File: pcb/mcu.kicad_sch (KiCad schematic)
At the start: 28 parts, among them CN9 2x5, IC2 STM32f103C8T, X1 H130B-8.000-18-3030-EXT-TR, X2 32.768K12.5PI/MC306

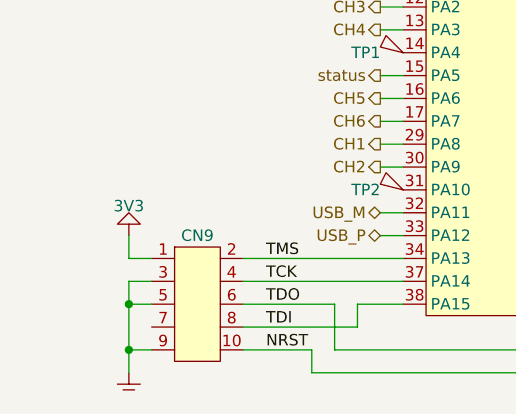
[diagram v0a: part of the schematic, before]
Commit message: worked on layout. changed JTAG pinout and changed it to bottomside test-points
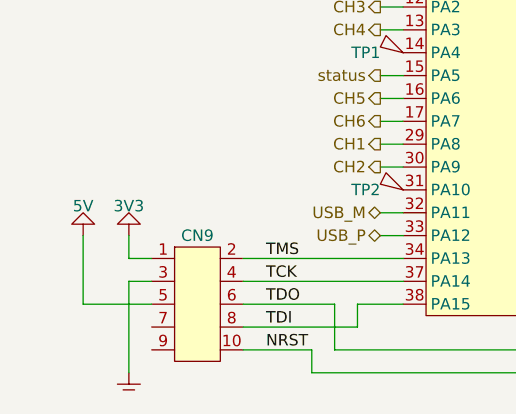
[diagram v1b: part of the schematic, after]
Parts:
- CN9: footprint pin_headers:2x5 -> pin_headers:2x5_test_points
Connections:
- net GND: no longer CN9.5, CN9.9
- new net 5V: CN9.5
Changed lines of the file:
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@@
   (junction (at 132.08 68.58) (diameter 0) (color 0 0 0 0)
   )
-  (junction (at 104.14 134.62) (diameter 0) (color 0 0 0 0)
-  )
   (junction (at 180.34 83.82) (diameter 0) (color 0 0 0 0)
   )
@@
   (junction (at 114.3 76.2) (diameter 0) (color 0 0 0 0)
   )
-  (junction (at 104.14 139.7) (diameter 0) (color 0 0 0 0)
-  )
   (junction (at 177.8 66.04) (diameter 0) (color 0 0 0 0)
   )
@@
     (stroke (width 0) (type default))
   )
-  (wire (pts (xy 104.14 139.7) (xy 106.68 139.7))
-    (stroke (width 0) (type default))
-  )
   (wire (pts (xy 114.3 73.66) (xy 114.3 76.2))
     (stroke (width 0) (type default))
@@
     (stroke (width 0) (type default))
   )
+  (wire (pts (xy 99.06 127) (xy 99.06 134.62))
+    (stroke (width 0) (type default))
+  )
   (wire (pts (xy 132.08 68.58) (xy 134.62 68.58))
     (stroke (width 0) (type default))
@@
     (stroke (width 0) (type default))
   )
-  (wire (pts (xy 104.14 134.62) (xy 106.68 134.62))
-    (stroke (width 0) (type default))
-  )
   (wire (pts (xy 165.1 66.04) (xy 177.8 66.04))
     (stroke (width 0) (type default))
@@
     (stroke (width 0) (type default))
   )
+  (wire (pts (xy 99.06 134.62) (xy 106.68 134.62))
+    (stroke (width 0) (type default))
+  )
   (wire (pts (xy 132.08 114.3) (xy 134.62 114.3))
     (stroke (width 0) (type default))
@@
     (stroke (width 0) (type default))
   )
-  (wire (pts (xy 104.14 132.08) (xy 104.14 134.62))
+  (wire (pts (xy 104.14 132.08) (xy 104.14 142.24))
     (stroke (width 0) (type default))
   )
@@
     (stroke (width 0) (type default))
   )
-  (wire (pts (xy 104.14 139.7) (xy 104.14 134.62))
-    (stroke (width 0) (type default))
-  )
   (wire (pts (xy 160.02 121.92) (xy 162.56 121.92))
     (stroke (width 0) (type default))
@@
   )
   (wire (pts (xy 185.42 83.82) (xy 187.96 83.82))
-    (stroke (width 0) (type default))
-  )
-  (wire (pts (xy 104.14 142.24) (xy 104.14 139.7))
     (stroke (width 0) (type default))
   )
@@
     )
   )
+  (symbol (lib_id "generic:5V") (at 99.06 127 0) (unit 1)
+    (in_bom yes) (on_board yes) (dnp no)
+    (property "Reference" "#5V03" (at 102.87 125.73 0)
+      (effects (font (size 1.27 1.27)) hide)
+    )
+    (property "Value" "5V" (at 99.06 124.46 0)
+      (effects (font (size 1.27 1.27)) (justify bottom))
+    )
+    (property "Footprint" "" (at 99.06 127 0)
+      (effects (font (size 1.27 1.27)) hide)
+    )
+    (property "Datasheet" "" (at 99.06 127 0)
+      (effects (font (size 1.27 1.27)) hide)
+    )
+    (pin "~")
+    (instances
+      (project "pcb"
+        (path "/6bb3bad6-1a89-4624-b34d-6ddda7dd16d2"
+          (reference "#5V03") (unit 1)
+        )
+        (path "/6bb3bad6-1a89-4624-b34d-6ddda7dd16d2/19469851-aeaf-466c-9786-c0d0ae531cf4"
+          (reference "#5V02") (unit 1)
+        )
+      )
+    )
+  )
   (symbol (lib_id "PCB:test_point") (at 180.34 114.3 0) (unit 1)
     (in_bom yes) (on_board yes) (dnp no) (fields_autoplaced)
@@
       (effects (font (size 1.27 1.27)) hide)
     )
-    (property "Footprint" "pin_headers:2x5" (at 106.68 129.54 0)
-      (effects (font (size 1.27 1.27)) hide)
-    )
+    (property "Footprint" "pin_headers:2x5_test_points" (at 106.68 129.54 0)
+      (effects (font (size 1.27 1.27)) hide)
+    )

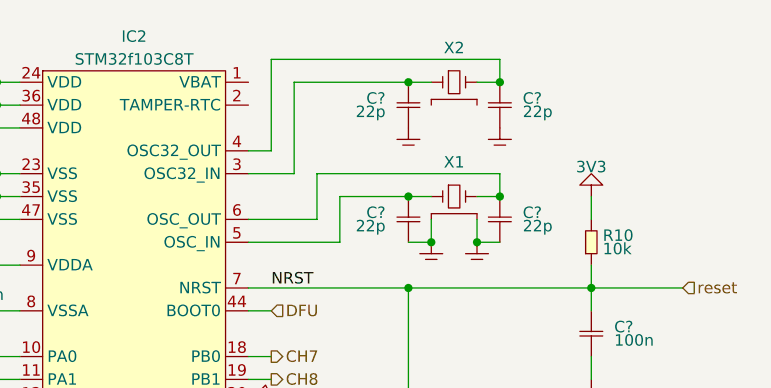
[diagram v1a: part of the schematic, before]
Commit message: removed RTC crystal, started routing
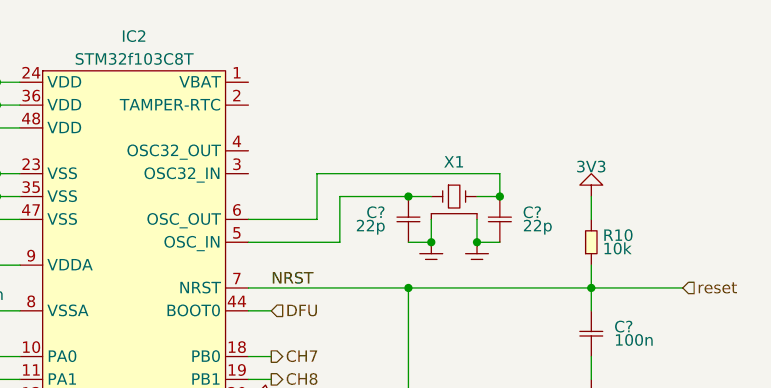
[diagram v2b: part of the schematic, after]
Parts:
- removed C? (x2): 22p, SMT:0603, symbol generic:C
- removed X2: 32.768K12.5PI/MC306, xtal:8x3.2, symbol oscillators:32.768K12.5PI/MC306
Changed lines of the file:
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@@
     (comment 1 "Microcontroller and programming headers")
   )
-  (junction (at 187.96 66.04) (diameter 0) (color 0 0 0 0)
-  )
   (junction (at 127 91.44) (diameter 0) (color 0 0 0 0)
   )
@@
   (junction (at 114.3 76.2) (diameter 0) (color 0 0 0 0)
   )
-  (junction (at 177.8 66.04) (diameter 0) (color 0 0 0 0)
-  )
   (junction (at 127 86.36) (diameter 0) (color 0 0 0 0)
   )
@@
     (stroke (width 0) (type default))
   )
-  (wire (pts (xy 160.02 73.66) (xy 162.56 73.66))
-    (stroke (width 0) (type default))
-  )
   (wire (pts (xy 127 139.7) (xy 175.26 139.7))
     (stroke (width 0) (type default))
@@
     (stroke (width 0) (type default))
   )
-  (wire (pts (xy 177.8 66.04) (xy 180.34 66.04))
-    (stroke (width 0) (type default))
-  )
   (wire (pts (xy 160.02 111.76) (xy 180.34 111.76))
     (stroke (width 0) (type default))
@@
     (stroke (width 0) (type default))
   )
-  (wire (pts (xy 165.1 76.2) (xy 165.1 66.04))
-    (stroke (width 0) (type default))
-  )
-  (wire (pts (xy 162.56 73.66) (xy 162.56 63.5))
-    (stroke (width 0) (type default))
-  )
   (wire (pts (xy 116.84 132.08) (xy 134.62 132.08))
     (stroke (width 0) (type default))
@@
     (stroke (width 0) (type default))
   )
-  (wire (pts (xy 165.1 66.04) (xy 177.8 66.04))
-    (stroke (width 0) (type default))
-  )
   (wire (pts (xy 177.8 78.74) (xy 180.34 78.74))
     (stroke (width 0) (type default))
   )
-  (wire (pts (xy 187.96 63.5) (xy 187.96 66.04))
-    (stroke (width 0) (type default))
-  )
   (wire (pts (xy 116.84 139.7) (xy 124.46 139.7))
     (stroke (width 0) (type default))
@@
     (stroke (width 0) (type default))
   )
-  (wire (pts (xy 162.56 63.5) (xy 187.96 63.5))
-    (stroke (width 0) (type default))
-  )
   (wire (pts (xy 167.64 81.28) (xy 160.02 81.28))
     (stroke (width 0) (type default))
@@
     (stroke (width 0) (type default))
   )
-  (wire (pts (xy 160.02 76.2) (xy 165.1 76.2))
-    (stroke (width 0) (type default))
-  )
   (wire (pts (xy 93.98 76.2) (xy 93.98 73.66))
     (stroke (width 0) (type default))
@@
   )
   (wire (pts (xy 185.42 83.82) (xy 187.96 83.82))
-    (stroke (width 0) (type default))
-  )
-  (wire (pts (xy 185.42 66.04) (xy 187.96 66.04))
     (stroke (width 0) (type default))
   )
@@
     )
   )
-  (symbol (lib_id "oscillators:32.768K12.5PI/MC306") (at 182.88 66.04 0) (unit 1)
-    (in_bom yes) (on_board yes) (dnp no)
-    (property "Reference" "X2" (at 182.88 62.23 0)
-      (effects (font (size 1.27 1.27)))
-    )
-    (property "Value" "32.768K12.5PI/MC306" (at 182.88 66.04 0)
-      (effects (font (size 1.27 1.27)) hide)
-    )
-    (property "Footprint" "xtal:8x3.2" (at 182.88 49.53 0)
-      (effects (font (size 1.27 1.27)) hide)
-    )
-    (property "Datasheet" "https://www.yic.com.tw/wp-content/uploads/2023/11/YIC-MC306-Series.pdf" (at 182.88 57.15 0)
-      (effects (font (size 1.27 1.27)) hide)
-    )
-    (property "MPN" "32.768K12.5PI/MC306" (at 182.88 52.07 0)
-      (effects (font (size 1.27 1.27)) hide)
-    )
-    (property "DigiKey" "3155-32.768K12.5PI/MC306CT-ND" (at 182.88 54.61 0)
-      (effects (font (size 1.27 1.27)) hide)
-    )
-    (pin "1")
-    (pin "2")
-    (pin "3")
-    (pin "4")
-    (instances
-      (project "pcb"
-        (path "/6bb3bad6-1a89-4624-b34d-6ddda7dd16d2/19469851-aeaf-466c-9786-c0d0ae531cf4"
-          (reference "X2") (unit 1)
-        )
-      )
-    )
-  )
   (symbol (lib_id "generic:C") (at 114.3 71.12 0) (unit 1)
     (in_bom yes) (on_board yes) (dnp no)
@@
     )
   )
-  (symbol (lib_id "generic:C") (at 177.8 68.58 0) (mirror y) (unit 1)
-    (in_bom yes) (on_board yes) (dnp no)
-    (property "Reference" "C?" (at 175.26 68.58 0)
+  (symbol (lib_id "generic:C") (at 187.96 81.28 0) (unit 1)
+    (in_bom yes) (on_board yes) (dnp no)
+    (property "Reference" "C?" (at 190.5 81.28 0)
       (effects (font (size 1.27 1.27)) (justify left bottom))
     )
-    (property "Value" "22p" (at 175.26 68.58 0)
+    (property "Value" "22p" (at 190.5 81.28 0)
       (effects (font (size 1.27 1.27)) (justify left top))
     )
-    (property "Footprint" "SMT:0603" (at 177.8 71.12 0)
-      (effects (font (size 1.27 1.27)) hide)
-    )
-    (property "Datasheet" "" (at 177.8 68.58 0)
+    (property "Footprint" "SMT:0603" (at 187.96 83.82 0)
+      (effects (font (size 1.27 1.27)) hide)
+    )
+    (property "Datasheet" "" (at 187.96 81.28 0)
       (effects (font (size 1.27 1.27)) hide)
     )
@@
         )
         (path "/6bb3bad6-1a89-4624-b34d-6ddda7dd16d2/19469851-aeaf-466c-9786-c0d0ae531cf4"
-          (reference "C18") (unit 1)
-        )
-      )
-    )
-  )
-  (symbol (lib_id "generic:C") (at 187.96 81.28 0) (unit 1)
-    (in_bom yes) (on_board yes) (dnp no)
-    (property "Reference" "C?" (at 190.5 81.28 0)
-      (effects (font (size 1.27 1.27)) (justify left bottom))
-    )
-    (property "Value" "22p" (at 190.5 81.28 0)
-      (effects (font (size 1.27 1.27)) (justify left top))
-    )
-    (property "Footprint" "SMT:0603" (at 187.96 83.82 0)
-      (effects (font (size 1.27 1.27)) hide)
-    )
-    (property "Datasheet" "" (at 187.96 81.28 0)
-      (effects (font (size 1.27 1.27)) hide)
-    )
-    (pin "1")
-    (pin "2")
-    (instances
-      (project "pcb"
-        (path "/6bb3bad6-1a89-4624-b34d-6ddda7dd16d2/bd5ce3a2-965f-4825-a529-9d15232fee93"
-          (reference "C?") (unit 1)
-        )
-        (path "/6bb3bad6-1a89-4624-b34d-6ddda7dd16d2/19469851-aeaf-466c-9786-c0d0ae531cf4"
           (reference "C16") (unit 1)
         )
@@
         (path "/6bb3bad6-1a89-4624-b34d-6ddda7dd16d2/19469851-aeaf-466c-9786-c0d0ae531cf4"
           (reference "#3V02") (unit 1)
-        )
-      )
-    )
-  )
-  (symbol (lib_id "generic:C") (at 187.96 68.58 0) (unit 1)
-    (in_bom yes) (on_board yes) (dnp no)
-    (property "Reference" "C?" (at 190.5 68.58 0)
-      (effects (font (size 1.27 1.27)) (justify left bottom))
-    )
-    (property "Value" "22p" (at 190.5 68.58 0)
-      (effects (font (size 1.27 1.27)) (justify left top))
-    )
-    (property "Footprint" "SMT:0603" (at 187.96 71.12 0)
-      (effects (font (size 1.27 1.27)) hide)
-    )
-    (property "Datasheet" "" (at 187.96 68.58 0)
-      (effects (font (size 1.27 1.27)) hide)
-    )
-    (pin "1")
-    (pin "2")
-    (instances
-      (project "pcb"
-        (path "/6bb3bad6-1a89-4624-b34d-6ddda7dd16d2/bd5ce3a2-965f-4825-a529-9d15232fee93"
-          (reference "C?") (unit 1)
-        )
-        (path "/6bb3bad6-1a89-4624-b34d-6ddda7dd16d2/19469851-aeaf-466c-9786-c0d0ae531cf4"
-          (reference "C19") (unit 1)
         )
       )
@@
     )
   )
-  (symbol (lib_id "generic:GND") (at 187.96 71.12 0) (unit 1)
-    (in_bom yes) (on_board yes) (dnp no) (fields_autoplaced)
-    (property "Reference" "#GND025" (at 191.77 69.85 0)
-      (effects (font (size 1.27 1.27)) hide)
-    )
-    (property "Value" "GND" (at 191.77 71.12 0)
-      (effects (font (size 1.27 1.27)) hide)
-    )
-    (property "Footprint" "" (at 187.96 71.12 0)
-      (effects (font (size 1.27 1.27)) hide)
-    )
-    (property "Datasheet" "" (at 187.96 71.12 0)
-      (effects (font (size 1.27 1.27)) hide)
-    )
-    (pin "~")
-    (instances
-      (project "pcb"
-        (path "/6bb3bad6-1a89-4624-b34d-6ddda7dd16d2/19469851-aeaf-466c-9786-c0d0ae531cf4"
-          (reference "#GND025") (unit 1)
-        )
-      )
-    )
-  )
   (symbol (lib_id "generic:GND") (at 116.84 93.98 0) (unit 1)
     (in_bom yes) (on_board yes) (dnp no) (fields_autoplaced)
@@
         )
       )
-    )
-  )
-  (symbol (lib_id "generic:GND") (at 177.8 71.12 0) (unit 1)
-    (in_bom yes) (on_board yes) (dnp no) (fields_autoplaced)
-    (property "Reference" "#GND024" (at 181.61 69.85 0)
-      (effects (font (size 1.27 1.27)) hide)
-    )
-    (property "Value" "GND" (at 181.61 71.12 0)
-      (effects (font (size 1.27 1.27)) hide)
-    )
-    (property "Footprint" "" (at 177.8 71.12 0)
-      (effects (font (size 1.27 1.27)) hide)
-    )
-    (property "Datasheet" "" (at 177.8 71.12 0)
-      (effects (font (size 1.27 1.27)) hide)
-    )
-    (pin "~")
-    (instances
-      (project "pcb"
-        (path "/6bb3bad6-1a89-4624-b34d-6ddda7dd16d2/19469851-aeaf-466c-9786-c0d0ae531cf4"
-          (reference "#GND024") (unit 1)
-        )
-      )

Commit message: routing completed
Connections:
- net USB_M renamed USB_N
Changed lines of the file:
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@@
     (effects (font (size 1.27 1.27)) (justify right))
   )
-  (hierarchical_label "USB_M" (shape bidirectional) (at 132.08 124.46 180) (fields_autoplaced)
+  (hierarchical_label "USB_N" (shape bidirectional) (at 132.08 124.46 180) (fields_autoplaced)
     (effects (font (size 1.27 1.27)) (justify right))
   )
